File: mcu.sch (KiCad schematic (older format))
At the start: 6 parts, among them IC1 BUQ2-ATXMEGA128A4U-A, U8 TAG-CONNECT-ATMEL-PDI-CONNECT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

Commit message: Add gps
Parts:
- C12, C13, C14, C15: value C -> 100n
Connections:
- net MOSI: now reaches IC1.15 (MOSI/XCK1/OC0CHS/OC1B/PC5)
- net MISO: now reaches IC1.16 (CLKRTC/MISO/RXD1/~OC0DLS~/PC6)
- net SCK: now reaches IC1.17 (EVOUT/CLKOUT/SCK/TXD1/OC0DHS/PC7)
- net D-: now reaches IC1.26 (PD6/D-/RXD1/MISO)
- net D+: now reaches IC1.27 (PD7/D+/TXD1/SCK/CLKOUT/EVOUT)
- net RX: now reaches IC1.32 (PE2/OC0C/RXD0)
- net TX: now reaches IC1.33 (PE3/OC0D/TXD0)
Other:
- note added: "SPI"
- note added: "USB"
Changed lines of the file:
@@
 $Descr A4 11693 8268
 encoding utf-8
-Sheet 9 10
+Sheet 9 11
 Title ""
 Date ""
@@
 P 3650 1900
 F 0 "C12" H 3650 2000 40  0000 L CNN
-F 1 "C" H 3656 1815 40  0000 L CNN
+F 1 "100n" H 3656 1815 40  0000 L CNN
 F 2 "" H 3688 1750 30  0001 C CNN
 F 3 "" H 3650 1900 60  0000 C CNN
@@
 P 3900 1900
 F 0 "C13" H 3900 2000 40  0000 L CNN
-F 1 "C" H 3906 1815 40  0000 L CNN
+F 1 "100n" H 3906 1815 40  0000 L CNN
 F 2 "" H 3938 1750 30  0001 C CNN
 F 3 "" H 3900 1900 60  0000 C CNN
@@
 P 4150 1900
 F 0 "C14" H 4150 2000 40  0000 L CNN
-F 1 "C" H 4156 1815 40  0000 L CNN
+F 1 "100n" H 4156 1815 40  0000 L CNN
 F 2 "" H 4188 1750 30  0001 C CNN
 F 3 "" H 4150 1900 60  0000 C CNN
@@
 P 4400 1900
 F 0 "C15" H 4400 2000 40  0000 L CNN
-F 1 "C" H 4406 1815 40  0000 L CNN
+F 1 "100n" H 4406 1815 40  0000 L CNN
 F 2 "" H 4438 1750 30  0001 C CNN
 F 3 "" H 4400 1900 60  0000 C CNN
@@
 $EndComp
 $Comp
-L GND #PWR14
+L GND #PWR20
 U 1 1 54464F33
 P 4100 1400
-F 0 "#PWR14" H 4100 1400 30  0001 C CNN
+F 0 "#PWR20" H 4100 1400 30  0001 C CNN
 F 1 "GND" H 4100 1330 30  0001 C CNN
 F 2 "" H 4100 1400 60  0000 C CNN
@@
 NoConn ~ 6300 2350
 $Comp
-L GND #PWR15
+L GND #PWR21
 U 1 1 54464F41
 P 7450 2500
-F 0 "#PWR15" H 7450 2500 30  0001 C CNN
+F 0 "#PWR21" H 7450 2500 30  0001 C CNN
 F 1 "GND" H 7450 2430 30  0001 C CNN
 F 2 "" H 7450 2500 60  0000 C CNN
@@
 $EndComp
 $Comp
-L GND #PWR13
+L GND #PWR19
 U 1 1 54464F47
 P 3900 5100
-F 0 "#PWR13" H 3900 5100 30  0001 C CNN
+F 0 "#PWR19" H 3900 5100 30  0001 C CNN
 F 1 "GND" H 3900 5030 30  0001 C CNN
 F 2 "" H 3900 5100 60  0000 C CNN
@@
 	4050 4900 4050 5000
 Connection ~ 3950 5000
+Text HLabel 3000 4400 0    60   Input ~ 0
+D-
+Text HLabel 3000 4500 0    60   Input ~ 0
+D+
+Text HLabel 5700 4300 2    60   Input ~ 0
+MOSI
+Text HLabel 5700 4400 2    60   Input ~ 0
+MISO
+Text HLabel 5700 4500 2    60   Input ~ 0
+SCK
+Text Notes 6150 4400 0    60   ~ 0
+SPI
+Text Notes 2550 4500 0    60   ~ 0
+USB
+Text HLabel 3000 3550 0    60   Input ~ 0
+RX
+Text HLabel 3000 3650 0    60   Input ~ 0
+TX
 $EndSCHEMATC

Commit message: More connections
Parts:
- added R6, R7: 1.5k, buq2:SM0603, symbol R
- C12, C13, C14, C15: footprint (none) -> buq2:SM0603
- IC1: footprint (none) -> buq2:BUQ2-TQFP44
- U8: footprint (none) -> buq2:TAG-CONNECT6
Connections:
- net I2C_SDA: now reaches IC1.10 (SDAIN/SDA/~OC0ALS~/OC0A/PC0)
- net I2C_SDA: now also R7.2
- net I2C_SCL: now reaches IC1.11 (SCLIN/SCL/XCK0/OC0AHS/OC0B/PC1)
- net I2C_SCL: now also R6.2
- net DISPLAY_INVERT: now reaches IC1.4 (AREFB/ADC8/PB0)
- net CLOCK_INT: now reaches IC1.42 (AC2/ADC2/PA2)
- net ACCELERATOR_INT: now reaches IC1.43 (AC3/ADC3/PA3)
- net BAROMETER_INT: now reaches IC1.44 (AC4/ADC4/PA4)
- net BUZZER_DRIVE: now reaches IC1.5 (ADC9/PB1)
- net MCU_VCC renamed VDD
- net VDD: now also R6.1, R7.1
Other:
- note added: "A port used for SPI CS\nand interrupts (PA0 = AREF?)"
- note added: "B port used for interrups\n(PB0 = AREF?)"
- moved on the sheet: U8
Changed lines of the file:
@@
 F 0 "IC1" H 3150 4700 40  0000 L BNN
 F 1 "BUQ2-ATXMEGA128A4U-A" H 4250 2150 40  0000 L BNN
-F 2 "" H 3900 3500 35  0000 C CIN
+F 2 "buq2:BUQ2-TQFP44" H 3900 3500 35  0001 C CIN
 F 3 "" H 3900 3500 60  0000 C CNN
 	1    3900 3500
@@
 L TAG-CONNECT-ATMEL-PDI-CONNECTOR U8
 U 1 1 54464F10
-P 6850 2350
-F 0 "U8" H 6800 1950 60  0000 C CNN
-F 1 "TAG-CONNECT-ATMEL-PDI-CONNECTOR" H 6850 2750 60  0000 C CNN
-F 2 "" H 6850 2350 60  0001 C CNN
-F 3 "" H 6850 2350 60  0000 C CNN
-	1    6850 2350
+P 6650 1450
+F 0 "U8" H 6600 1050 60  0000 C CNN
+F 1 "TAG-CONNECT-ATMEL-PDI-CONNECTOR" H 6650 1850 60  0000 C CNN
+F 2 "buq2:TAG-CONNECT6" H 6650 1450 60  0001 C CNN
+F 3 "" H 6650 1450 60  0000 C CNN
+	1    6650 1450
 	1    0    0    -1
 $EndComp
@@
 F 0 "C12" H 3650 2000 40  0000 L CNN
 F 1 "100n" H 3656 1815 40  0000 L CNN
-F 2 "" H 3688 1750 30  0001 C CNN
+F 2 "buq2:SM0603" H 3688 1750 30  0001 C CNN
 F 3 "" H 3650 1900 60  0000 C CNN
 	1    3650 1900
@@
 F 0 "C13" H 3900 2000 40  0000 L CNN
 F 1 "100n" H 3906 1815 40  0000 L CNN
-F 2 "" H 3938 1750 30  0001 C CNN
+F 2 "buq2:SM0603" H 3938 1750 30  0001 C CNN
 F 3 "" H 3900 1900 60  0000 C CNN
 	1    3900 1900
@@
 F 0 "C14" H 4150 2000 40  0000 L CNN
 F 1 "100n" H 4156 1815 40  0000 L CNN
-F 2 "" H 4188 1750 30  0001 C CNN
+F 2 "buq2:SM0603" H 4188 1750 30  0001 C CNN
 F 3 "" H 4150 1900 60  0000 C CNN
 	1    4150 1900
@@
 F 0 "C15" H 4400 2000 40  0000 L CNN
 F 1 "100n" H 4406 1815 40  0000 L CNN
-F 2 "" H 4438 1750 30  0001 C CNN
+F 2 "buq2:SM0603" H 4438 1750 30  0001 C CNN
 F 3 "" H 4400 1900 60  0000 C CNN
 	1    4400 1900
@@
 $EndComp
 $Comp
-L GND #PWR20
+L GND #PWR021
 U 1 1 54464F33
 P 4100 1400
-F 0 "#PWR20" H 4100 1400 30  0001 C CNN
+F 0 "#PWR021" H 4100 1400 30  0001 C CNN
 F 1 "GND" H 4100 1330 30  0001 C CNN
 F 2 "" H 4100 1400 60  0000 C CNN
@@
 	-1   0    0    1
 $EndComp
-Text GLabel 6300 2200 0    39   Input ~ 0
-PDI_DATA
-Text GLabel 6300 2500 0    39   Input ~ 0
-PDI_CLK
-Text GLabel 7350 2200 2    39   Input ~ 0
-MCU_VCC
-Text GLabel 3650 2100 0    39   Input ~ 0
-MCU_VCC
-Text GLabel 3000 2600 0    39   Input ~ 0
-PDI_DATA
-Text GLabel 3000 2500 0    39   Input ~ 0
-PDI_CLK
-NoConn ~ 7350 2350
-NoConn ~ 6300 2350
-$Comp
-L GND #PWR21
+NoConn ~ 7150 1450
+NoConn ~ 6100 1450
+$Comp
+L GND #PWR022
 U 1 1 54464F41
-P 7450 2500
-F 0 "#PWR21" H 7450 2500 30  0001 C CNN
-F 1 "GND" H 7450 2430 30  0001 C CNN
-F 2 "" H 7450 2500 60  0000 C CNN
-F 3 "" H 7450 2500 60  0000 C CNN
-	1    7450 2500
+P 7250 1600
+F 0 "#PWR022" H 7250 1600 30  0001 C CNN
+F 1 "GND" H 7250 1530 30  0001 C CNN
+F 2 "" H 7250 1600 60  0000 C CNN
+F 3 "" H 7250 1600 60  0000 C CNN
+	1    7250 1600
 	0    -1   -1   0
 $EndComp
 $Comp
-L GND #PWR19
+L GND #PWR023
 U 1 1 54464F47
 P 3900 5100
-F 0 "#PWR19" H 3900 5100 30  0001 C CNN
+F 0 "#PWR023" H 3900 5100 30  0001 C CNN
 F 1 "GND" H 3900 5030 30  0001 C CNN
 F 2 "" H 3900 5100 60  0000 C CNN
@@
 Connection ~ 3900 1700
 Wire Wire Line
-	7450 2500 7350 2500
+	7250 1600 7150 1600
 Wire Wire Line
 	3900 5000 3900 5100
@@
 Text HLabel 3000 3650 0    60   Input ~ 0
 TX
+$Comp
+L R R6
+U 1 1 54632D6A
+P 8150 3800
+F 0 "R6" V 8230 3800 40  0000 C CNN
+F 1 "1.5k" V 8157 3801 40  0000 C CNN
+F 2 "buq2:SM0603" V 8080 3800 30  0001 C CNN
+F 3 "" H 8150 3800 30  0000 C CNN
+	1    8150 3800
+	1    0    0    -1
+$EndComp
+$Comp
+L R R7
+U 1 1 54632DC5
+P 8300 3800
+F 0 "R7" V 8380 3800 40  0000 C CNN
+F 1 "1.5k" V 8307 3801 40  0000 C CNN
+F 2 "buq2:SM0603" V 8230 3800 30  0001 C CNN
+F 3 "" H 8300 3800 30  0000 C CNN
+	1    8300 3800
+	1    0    0    -1
+$EndComp
+Text HLabel 8300 4050 2    60   Input ~ 0
+I2C_SDA
+Text HLabel 8150 4250 2    60   Input ~ 0
+I2C_SCL
+Text HLabel 3650 2100 0    60   Input ~ 0
+VDD
+Text HLabel 8250 3400 1    60   Input ~ 0
+VDD
+Wire Wire Line
+	8150 3400 8300 3400
+Wire Wire Line
+	8150 3400 8150 3550
+Wire Wire Line
+	8300 3400 8300 3550
+Wire Wire Line
+	8150 4050 8150 4250
+Text Notes 6900 2550 0    60   ~ 0
+A port used for SPI CS\nand interrupts (PA0 = AREF?)
+Text Notes 6850 3400 0    60   ~ 0
+B port used for interrups\n(PB0 = AREF?)
+Text HLabel 5700 3800 2    60   Input ~ 0
+I2C_SDA
+Text HLabel 5700 3900 2    60   Input ~ 0
+I2C_SCL
+Text Label 6100 1300 2    60   ~ 0
+PDI_DATA
+Text Label 6100 1600 2    60   ~ 0
+PDI_CLK
+Text HLabel 7150 1300 2    60   Input ~ 0
+VDD
+Text Label 3000 2500 2    60   ~ 0
+PDI_CLK
+Text Label 3000 2600 2    60   ~ 0
+PDI_DATA
+Text HLabel 5700 3350 2    60   Input ~ 0
+DISPLAY_INVERT
+Text HLabel 5700 3450 2    60   Input ~ 0
+BUZZER_DRIVE
+Text HLabel 5700 2700 2    60   Input ~ 0
+CLOCK_INT
+Text HLabel 5700 2800 2    60   Input ~ 0
+ACCELERATOR_INT
+Text HLabel 5700 2900 2    60   Input ~ 0
+BAROMETER_INT
 $EndSCHEMATC

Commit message: Add flash and ram. Some connections and DRC cleaning
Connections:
- net SD_CARD_DETECT: now reaches IC1.1 (AC5/ADC5/PA5)
- net GPS_PULSE_PER_SECOND: now reaches IC1.2 (AC1OUT/AC6/ADC6/PA6)
- net CSn_FLASH: now reaches IC1.20 (PD0/OC0A)
- net CSn_RAM: now reaches IC1.21 (PD1/OC0B/XCK0)
- net CSp_DISPLAY: now reaches IC1.22 (PD2/OC0C/RXD0)
- net CSn_SD_CARD: now reaches IC1.23 (PD3/OC0D/TXD0)
- no-connect marks 2 -> 16
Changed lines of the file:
@@
 $Descr A4 11693 8268
 encoding utf-8
-Sheet 9 12
+Sheet 9 13
 Title ""
 Date ""
@@
 $EndComp
 $Comp
-L GND #PWR021
+L GND #PWR022
 U 1 1 54464F33
 P 4100 1400
-F 0 "#PWR021" H 4100 1400 30  0001 C CNN
+F 0 "#PWR022" H 4100 1400 30  0001 C CNN
 F 1 "GND" H 4100 1330 30  0001 C CNN
 F 2 "" H 4100 1400 60  0000 C CNN
@@
 NoConn ~ 6100 1450
 $Comp
-L GND #PWR022
+L GND #PWR023
 U 1 1 54464F41
 P 7250 1600
-F 0 "#PWR022" H 7250 1600 30  0001 C CNN
+F 0 "#PWR023" H 7250 1600 30  0001 C CNN
 F 1 "GND" H 7250 1530 30  0001 C CNN
 F 2 "" H 7250 1600 60  0000 C CNN
@@
 $EndComp
 $Comp
-L GND #PWR023
+L GND #PWR024
 U 1 1 54464F47
 P 3900 5100
-F 0 "#PWR023" H 3900 5100 30  0001 C CNN
+F 0 "#PWR024" H 3900 5100 30  0001 C CNN
 F 1 "GND" H 3900 5030 30  0001 C CNN
 F 2 "" H 3900 5100 60  0000 C CNN
@@
 Text HLabel 5700 2900 2    60   Input ~ 0
 BAROMETER_INT
+Text HLabel 3000 3800 0    60   Input ~ 0
+CSn_FLASH
+Text HLabel 3000 3900 0    60   Input ~ 0
+CSn_RAM
+Text HLabel 3000 4000 0    60   Input ~ 0
+CSp_DISPLAY
+Text HLabel 3000 4100 0    60   Input ~ 0
+CSn_SD_CARD
+Text HLabel 5700 3000 2    60   Input ~ 0
+SD_CARD_DETECT
+NoConn ~ 3000 4300
+NoConn ~ 3000 3450
+NoConn ~ 3000 3350
+NoConn ~ 3000 3200
+NoConn ~ 3000 3100
+NoConn ~ 5700 2500
+NoConn ~ 5700 2600
+NoConn ~ 5700 3200
+NoConn ~ 5700 3550
+NoConn ~ 5700 3650
+NoConn ~ 5700 4000
+NoConn ~ 5700 4100
+NoConn ~ 5700 4200
+NoConn ~ 3000 4200
+Text HLabel 5700 3100 2    60   Input ~ 0
+GPS_PULSE_PER_SECOND
 $EndSCHEMATC

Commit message: Add buttons. Fix DRC. Add antenna
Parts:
- renumbered R6 to R5, R7 to R6, U8 to U9, C13 to XC10, C14 to XC11, C15 to XC12, C12 to XC9
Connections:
- net ACCELERATOR_INT: now also IC1.41 (AC1/ADC1/PA1); no longer IC1.43 (AC3/ADC3/PA3)
- net BAROMETER_INT: now also IC1.42 (AC2/ADC2/PA2); no longer IC1.44 (AC4/ADC4/PA4)
- net BUZZER_DRIVE: now also IC1.7 (DAC1/ACD11/PB3); no longer IC1.5 (ADC9/PB1)
- net CLOCK_INT: now also IC1.40 (AREFA/AC0/ADC0/PA0); no longer IC1.42 (AC2/ADC2/PA2)
- net DISPLAY_INVERT: now also IC1.6 (DAC0/ADC10/PB2); no longer IC1.4 (AREFB/ADC8/PB0)
- net GPS_PULSE_PER_SECOND: now also IC1.44 (AC4/ADC4/PA4); no longer IC1.2 (AC1OUT/AC6/ADC6/PA6)
- net SD_CARD_DETECT: now also IC1.43 (AC3/ADC3/PA3); no longer IC1.1 (AC5/ADC5/PA5)
- net BUTTON_LEFT: now reaches IC1.3 (AC0OUT/AC7/ADC7/PA7)
- new net BUTTON_CENTER: IC1.5 (ADC9/PB1)
- new net BUTTON_DOWN: IC1.2 (AC1OUT/AC6/ADC6/PA6)
- new net BUTTON_RIGHT: IC1.4 (AREFB/ADC8/PB0)
- new net BUTTON_UP: IC1.1 (AC5/ADC5/PA5)
- no-connect marks 16 -> 11
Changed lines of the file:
@@
 $Descr A4 11693 8268
 encoding utf-8
-Sheet 9 13
+Sheet 9 14
 Title ""
 Date ""
@@
 $EndComp
 $Comp
-L TAG-CONNECT-ATMEL-PDI-CONNECTOR U8
+L TAG-CONNECT-ATMEL-PDI-CONNECTOR U9
 U 1 1 54464F10
 P 6650 1450
-F 0 "U8" H 6600 1050 60  0000 C CNN
+F 0 "U9" H 6600 1050 60  0000 C CNN
 F 1 "TAG-CONNECT-ATMEL-PDI-CONNECTOR" H 6650 1850 60  0000 C CNN
 F 2 "buq2:TAG-CONNECT6" H 6650 1450 60  0001 C CNN
@@
 $EndComp
 $Comp
-L C C12
+L C XC9
 U 1 1 54464F17
 P 3650 1900
-F 0 "C12" H 3650 2000 40  0000 L CNN
+F 0 "XC9" H 3650 2000 40  0000 L CNN
 F 1 "100n" H 3656 1815 40  0000 L CNN
 F 2 "buq2:SM0603" H 3688 1750 30  0001 C CNN
@@
 $EndComp
 $Comp
-L C C13
+L C XC10
 U 1 1 54464F1E
 P 3900 1900
-F 0 "C13" H 3900 2000 40  0000 L CNN
+F 0 "XC10" H 3900 2000 40  0000 L CNN
 F 1 "100n" H 3906 1815 40  0000 L CNN
 F 2 "buq2:SM0603" H 3938 1750 30  0001 C CNN
@@
 $EndComp
 $Comp
-L C C14
+L C XC11
 U 1 1 54464F25
 P 4150 1900
-F 0 "C14" H 4150 2000 40  0000 L CNN
+F 0 "XC11" H 4150 2000 40  0000 L CNN
 F 1 "100n" H 4156 1815 40  0000 L CNN
 F 2 "buq2:SM0603" H 4188 1750 30  0001 C CNN
@@
 $EndComp
 $Comp
-L C C15
+L C XC12
 U 1 1 54464F2C
 P 4400 1900
-F 0 "C15" H 4400 2000 40  0000 L CNN
+F 0 "XC12" H 4400 2000 40  0000 L CNN
 F 1 "100n" H 4406 1815 40  0000 L CNN
 F 2 "buq2:SM0603" H 4438 1750 30  0001 C CNN
@@
 $EndComp
 $Comp
-L GND #PWR022
+L GND #PWR025
 U 1 1 54464F33
 P 4100 1400
-F 0 "#PWR022" H 4100 1400 30  0001 C CNN
+F 0 "#PWR025" H 4100 1400 30  0001 C CNN
 F 1 "GND" H 4100 1330 30  0001 C CNN
 F 2 "" H 4100 1400 60  0000 C CNN
@@
 NoConn ~ 6100 1450
 $Comp
-L GND #PWR023
+L GND #PWR026
 U 1 1 54464F41
 P 7250 1600
-F 0 "#PWR023" H 7250 1600 30  0001 C CNN
+F 0 "#PWR026" H 7250 1600 30  0001 C CNN
 F 1 "GND" H 7250 1530 30  0001 C CNN
 F 2 "" H 7250 1600 60  0000 C CNN
@@
 $EndComp
 $Comp
-L GND #PWR024
+L GND #PWR027
 U 1 1 54464F47
 P 3900 5100
-F 0 "#PWR024" H 3900 5100 30  0001 C CNN
+F 0 "#PWR027" H 3900 5100 30  0001 C CNN
 F 1 "GND" H 3900 5030 30  0001 C CNN
 F 2 "" H 3900 5100 60  0000 C CNN
@@
 TX
 $Comp
-L R R6
+L R R5
 U 1 1 54632D6A
 P 8150 3800
-F 0 "R6" V 8230 3800 40  0000 C CNN
+F 0 "R5" V 8230 3800 40  0000 C CNN
 F 1 "1.5k" V 8157 3801 40  0000 C CNN
 F 2 "buq2:SM0603" V 8080 3800 30  0001 C CNN
@@
 $EndComp
 $Comp
-L R R7
+L R R6
 U 1 1 54632DC5
 P 8300 3800
-F 0 "R7" V 8380 3800 40  0000 C CNN
+F 0 "R6" V 8380 3800 40  0000 C CNN
 F 1 "1.5k" V 8307 3801 40  0000 C CNN
 F 2 "buq2:SM0603" V 8230 3800 30  0001 C CNN
@@
 Text Label 3000 2600 2    60   ~ 0
 PDI_DATA
-Text HLabel 5700 3350 2    60   Input ~ 0
+Text HLabel 5700 3550 2    60   Input ~ 0
 DISPLAY_INVERT
-Text HLabel 5700 3450 2    60   Input ~ 0
+Text HLabel 5700 3650 2    60   Input ~ 0
 BUZZER_DRIVE
+Text HLabel 5700 2500 2    60   Input ~ 0
+CLOCK_INT
+Text HLabel 5700 2600 2    60   Input ~ 0
+ACCELERATOR_INT
 Text HLabel 5700 2700 2    60   Input ~ 0
-CLOCK_INT
-Text HLabel 5700 2800 2    60   Input ~ 0
-ACCELERATOR_INT
-Text HLabel 5700 2900 2    60   Input ~ 0
 BAROMETER_INT
 Text HLabel 3000 3800 0    60   Input ~ 0
@@
 Text HLabel 3000 4100 0    60   Input ~ 0
 CSn_SD_CARD
-Text HLabel 5700 3000 2    60   Input ~ 0
+Text HLabel 5700 2800 2    60   Input ~ 0
 SD_CARD_DETECT
 NoConn ~ 3000 4300
@@
 NoConn ~ 3000 3200
 NoConn ~ 3000 3100
-NoConn ~ 5700 2500
-NoConn ~ 5700 2600
-NoConn ~ 5700 3200
-NoConn ~ 5700 3550
-NoConn ~ 5700 3650
 NoConn ~ 5700 4000
 NoConn ~ 5700 4100
 NoConn ~ 5700 4200
 NoConn ~ 3000 4200
+Text HLabel 5700 2900 2    60   Input ~ 0
+GPS_PULSE_PER_SECOND
+Text HLabel 5700 3000 2    60   Input ~ 0
+BUTTON_UP
 Text HLabel 5700 3100 2    60   Input ~ 0
-GPS_PULSE_PER_SECOND
+BUTTON_DOWN
+Text HLabel 5700 3200 2    60   Input ~ 0
+BUTTON_LEFT
+Text HLabel 5700 3350 2    60   Input ~ 0
+BUTTON_RIGHT
+Text HLabel 5700 3450 2    60   Input ~ 0
+BUTTON_CENTER
 $EndSCHEMATC

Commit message: Little bit layout
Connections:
- net BUTTON_CENTER: now also IC1.3 (AC0OUT/AC7/ADC7/PA7); no longer IC1.5 (ADC9/PB1)
- net BUTTON_DOWN: now also IC1.5 (ADC9/PB1); no longer IC1.2 (AC1OUT/AC6/ADC6/PA6)
- net BUTTON_LEFT: now also IC1.2 (AC1OUT/AC6/ADC6/PA6); no longer IC1.3 (AC0OUT/AC7/ADC7/PA7)
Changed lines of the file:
@@
 Text HLabel 5700 3000 2    60   Input ~ 0
 BUTTON_UP
+Text HLabel 5700 3450 2    60   Input ~ 0
+BUTTON_DOWN
 Text HLabel 5700 3100 2    60   Input ~ 0
-BUTTON_DOWN
-Text HLabel 5700 3200 2    60   Input ~ 0
 BUTTON_LEFT
 Text HLabel 5700 3350 2    60   Input ~ 0
 BUTTON_RIGHT
-Text HLabel 5700 3450 2    60   Input ~ 0
+Text HLabel 5700 3200 2    60   Input ~ 0
 BUTTON_CENTER
 $EndSCHEMATC

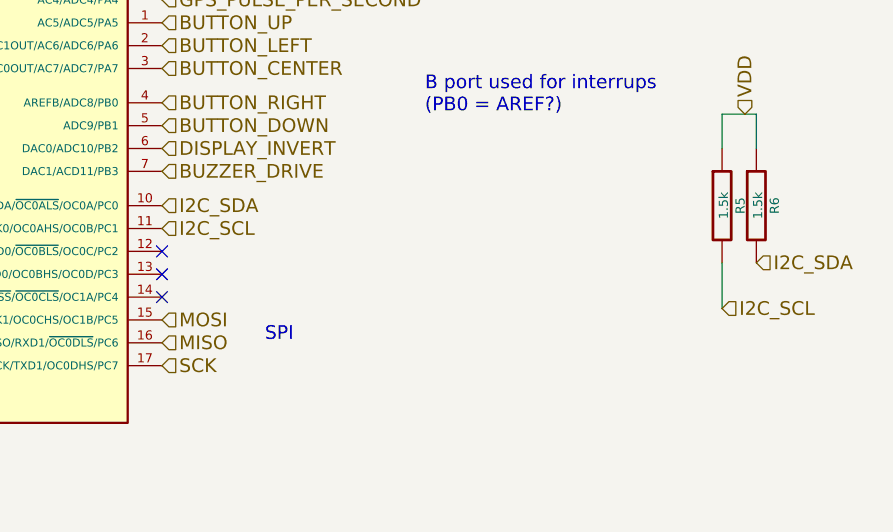
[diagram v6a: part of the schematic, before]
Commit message: Before making larger board. - Changed GPS module
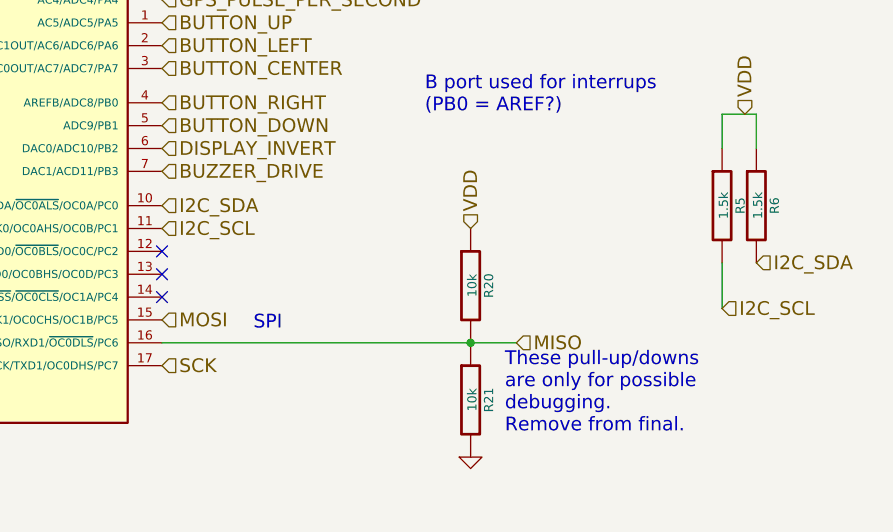
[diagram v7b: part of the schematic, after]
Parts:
- added R20, R21: 10k, symbol R
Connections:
- net GND: now also R21.2
- net MISO: now also R20.2, R21.1
- net VDD: now also R20.1
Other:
- note added: "These pull-up/downs\nare only for possible\ndebugging.\nRemove from final."
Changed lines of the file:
@@
 Text HLabel 5700 4300 2    60   Input ~ 0
 MOSI
-Text HLabel 5700 4400 2    60   Input ~ 0
+Text HLabel 7250 4400 2    60   Input ~ 0
 MISO
 Text HLabel 5700 4500 2    60   Input ~ 0
 SCK
-Text Notes 6150 4400 0    60   ~ 0
+Text Notes 6100 4350 0    60   ~ 0
 SPI
 Text Notes 2550 4500 0    60   ~ 0
@@
 Text HLabel 5700 3200 2    60   Input ~ 0
 BUTTON_CENTER
+$Comp
+L R R20
+U 1 1 547A08E0
+P 7050 4150
+F 0 "R20" V 7130 4150 40  0000 C CNN
+F 1 "10k" V 7057 4151 40  0000 C CNN
+F 2 "" V 6980 4150 30  0000 C CNN
+F 3 "" H 7050 4150 30  0000 C CNN
+	1    7050 4150
+	1    0    0    -1
+$EndComp
+$Comp
+L R R21
+U 1 1 547A090C
+P 7050 4650
+F 0 "R21" V 7130 4650 40  0000 C CNN
+F 1 "10k" V 7057 4651 40  0000 C CNN
+F 2 "" V 6980 4650 30  0000 C CNN
+F 3 "" H 7050 4650 30  0000 C CNN
+	1    7050 4650
+	1    0    0    -1
+$EndComp
+$Comp
+L GND #PWR028
+U 1 1 547A0947
+P 7050 4900
+F 0 "#PWR028" H 7050 4900 30  0001 C CNN
+F 1 "GND" H 7050 4830 30  0001 C CNN
+F 2 "" H 7050 4900 60  0000 C CNN
+F 3 "" H 7050 4900 60  0000 C CNN
+	1    7050 4900
+	1    0    0    -1
+$EndComp
+Text HLabel 7050 3900 1    60   Input ~ 0
+VDD
+Wire Wire Line
+	5700 4400 7250 4400
+Connection ~ 7050 4400
+Text Notes 7200 4800 0    60   ~ 0
+These pull-up/downs\nare only for possible\ndebugging.\nRemove from final.
 $EndSCHEMATC

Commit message: Before adding proper reset and battery monitor
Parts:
- R20, R21: footprint (none) -> buq2:SM0603
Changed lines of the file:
@@
 F 0 "R20" V 7130 4150 40  0000 C CNN
 F 1 "10k" V 7057 4151 40  0000 C CNN
-F 2 "" V 6980 4150 30  0000 C CNN
+F 2 "buq2:SM0603" V 6980 4150 30  0001 C CNN
 F 3 "" H 7050 4150 30  0000 C CNN
 	1    7050 4150
@@
 F 0 "R21" V 7130 4650 40  0000 C CNN
 F 1 "10k" V 7057 4651 40  0000 C CNN
-F 2 "" V 6980 4650 30  0000 C CNN
+F 2 "buq2:SM0603" V 6980 4650 30  0001 C CNN
 F 3 "" H 7050 4650 30  0000 C CNN
 	1    7050 4650
